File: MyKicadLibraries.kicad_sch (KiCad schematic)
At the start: 6 parts, among them U1 radio-receiver, U2 TP4056, U3 LilygoSIMT7000G, U4 esp-01m, U5 relais_module, U6 ESP-01

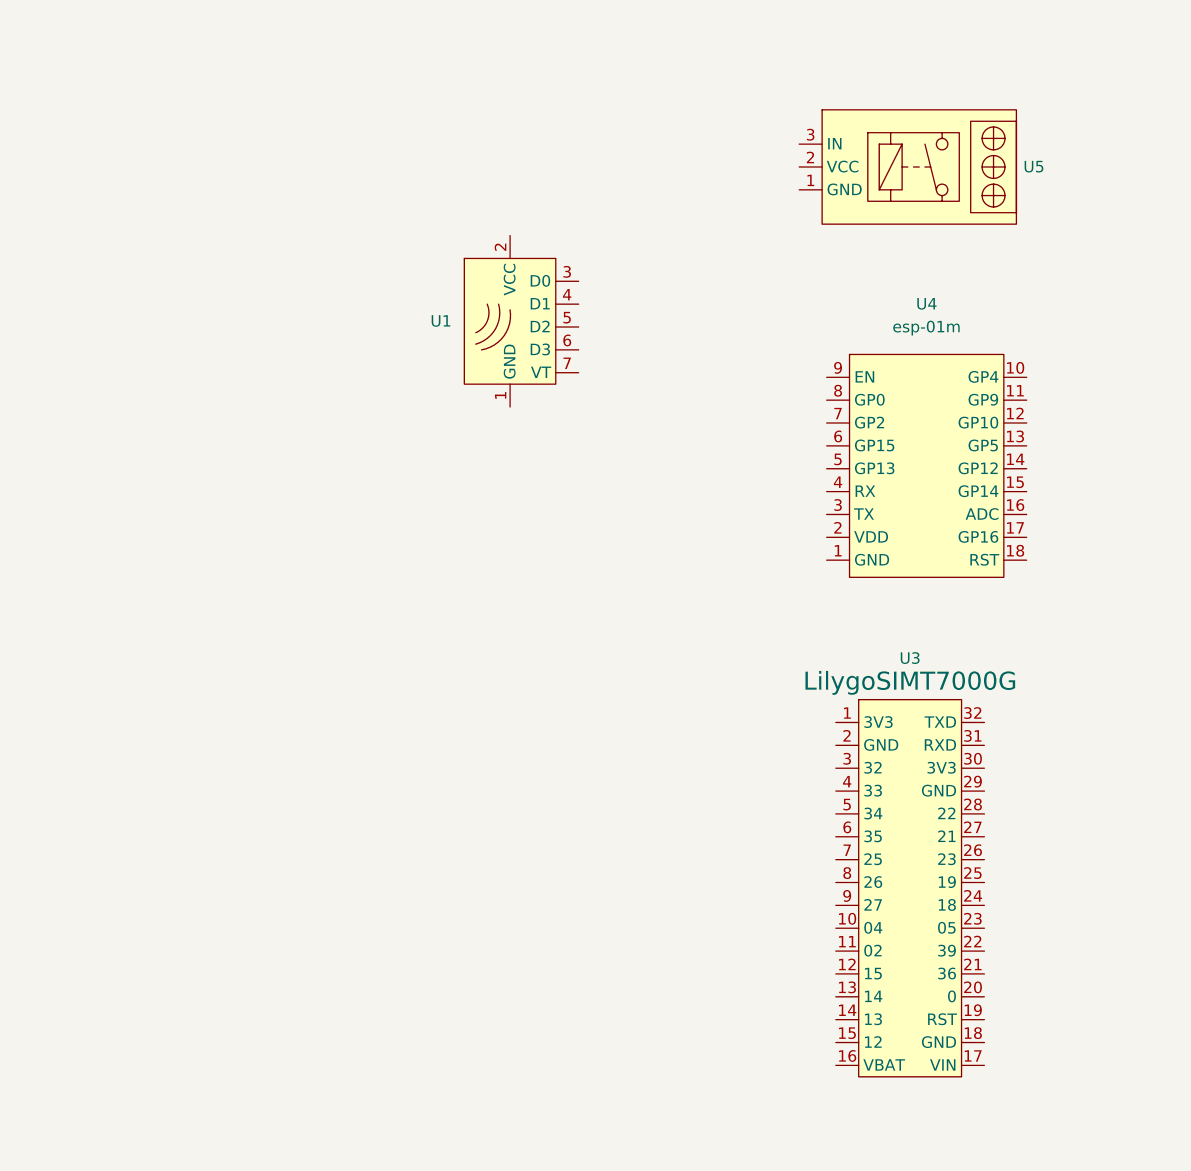
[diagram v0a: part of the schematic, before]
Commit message: Add dcdc module and add a breakout board
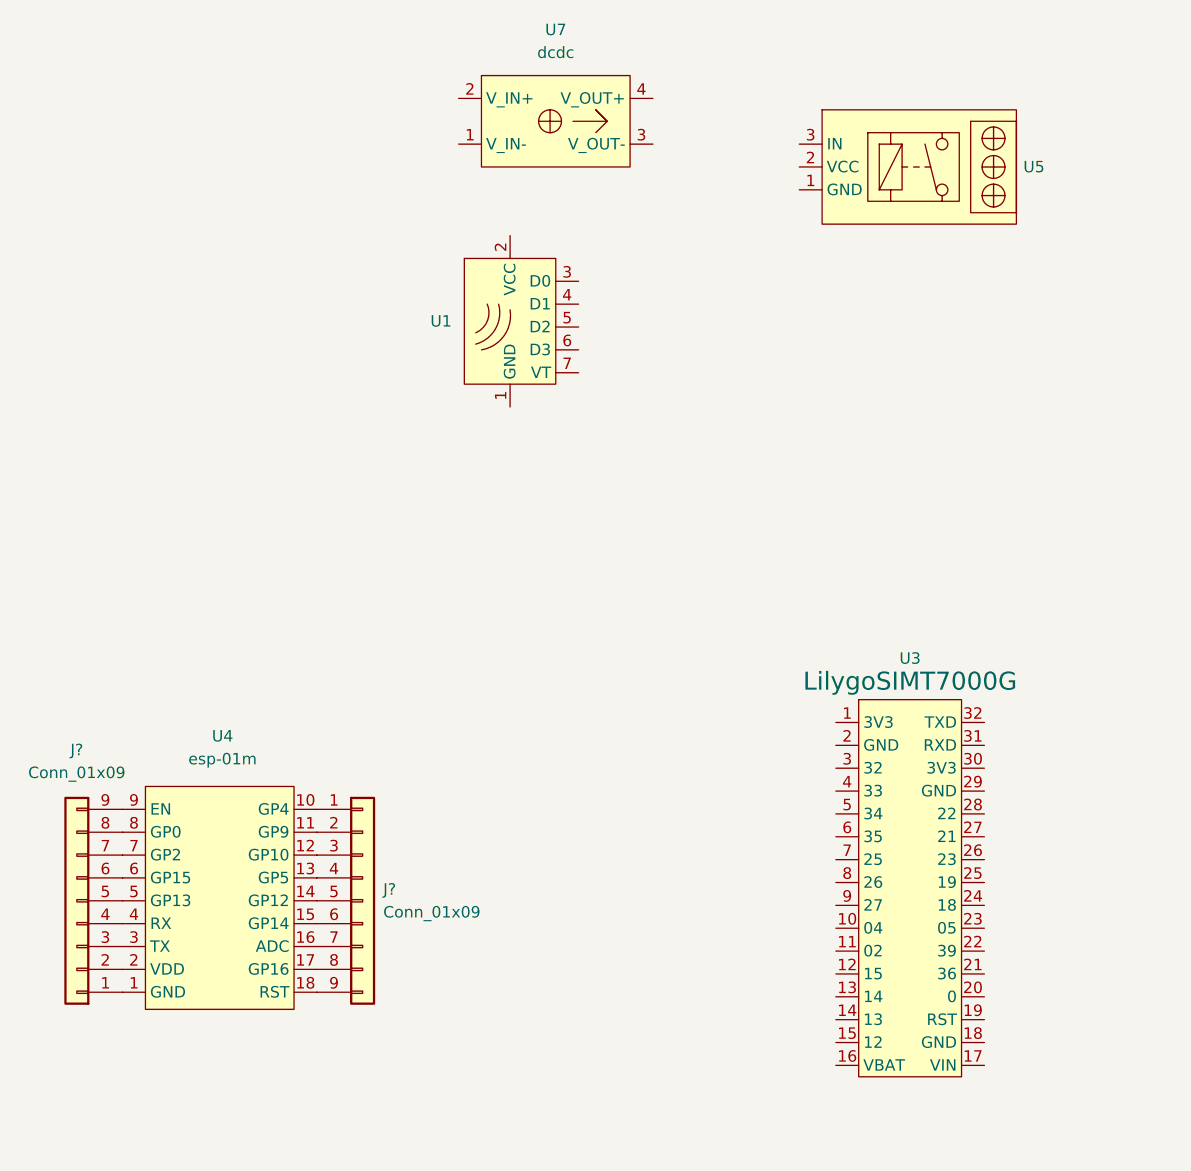
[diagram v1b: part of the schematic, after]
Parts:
- added J? (x2): Conn_01x09, connector 2.54:PinHeader_1x09_P2.54mm_Vertical, symbol connectors:Conn_01x09
- added U7: dcdc, dcdc:dcdc, symbol dcdc:dcdc
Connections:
- net at U4.1 (GND): now also J?.1 (Pin_1)
- net at U4.10 (GP4): now also J?.1 (Pin_1)
- net at U4.11 (GP9): now also J?.2 (Pin_2)
- net at U4.12 (GP10): now also J?.3 (Pin_3)
- net at U4.13 (GP5): now also J?.4 (Pin_4)
- net at U4.14 (GP12): now also J?.5 (Pin_5)
- net at U4.15 (GP14): now also J?.6 (Pin_6)
- net at U4.16 (ADC): now also J?.7 (Pin_7)
- net at U4.17 (GP16): now also J?.8 (Pin_8)
- net at U4.18 (RST): now also J?.9 (Pin_9)
- net at U4.2 (VDD): now also J?.2 (Pin_2)
- net at U4.3 (TX): now also J?.3 (Pin_3)
- net at U4.4 (RX): now also J?.4 (Pin_4)
- net at U4.5 (GP13): now also J?.5 (Pin_5)
- net at U4.6 (GP15): now also J?.6 (Pin_6)
- net at U4.7 (GP2): now also J?.7 (Pin_7)
- net at U4.8 (GP0): now also J?.8 (Pin_8)
- net at U4.9 (EN): now also J?.9 (Pin_9)
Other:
- moved on the sheet: U4
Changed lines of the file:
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@@
 (kicad_sch (version 20211123) (generator eeschema)
   (paper "A4")
-  (symbol (lib_id "esp-01m:esp-01m") (at 130.556 66.548 0) (unit 1)
-    (in_bom yes) (on_board yes) (fields_autoplaced)
-    (property "Reference" "U4" (id 0) (at 131.5085 48.26 0))
-    (property "Value" "esp-01m" (id 1) (at 131.5085 50.8 0))
-    (property "Footprint" "esp-01m:esp-01m" (id 2) (at 110.236 22.098 0)
-      (effects (font (size 1.27 1.27)) hide)
-    )
-    (property "Datasheet" "" (id 3) (at 110.236 22.098 0)
+  (symbol (lib_id "esp-01m:esp-01m") (at 52.324 114.554 0) (unit 1)
+    (in_bom yes) (on_board yes) (fields_autoplaced)
+    (property "Reference" "U4" (id 0) (at 53.2765 96.266 0))
+    (property "Value" "esp-01m" (id 1) (at 53.2765 98.806 0))
+    (property "Footprint" "esp-01m:esp-01m" (id 2) (at 32.004 70.104 0)
+      (effects (font (size 1.27 1.27)) hide)
+    )
+    (property "Datasheet" "" (id 3) (at 32.004 70.104 0)
       (effects (font (size 1.27 1.27)) hide)
     )
@@
     (pin "9")
   )
+  (symbol (lib_id "connectors:Conn_01x09") (at 68.834 114.554 0) (unit 1)
+    (in_bom yes) (on_board yes) (fields_autoplaced)
+    (property "Reference" "J?" (id 0) (at 71.12 113.2839 0)
+      (effects (font (size 1.27 1.27)) (justify left))
+    )
+    (property "Value" "Conn_01x09" (id 1) (at 71.12 115.8239 0)
+      (effects (font (size 1.27 1.27)) (justify left))
+    )
+    (property "Footprint" "connector 2.54:PinHeader_1x09_P2.54mm_Vertical" (id 2) (at 68.834 114.554 0)
+      (effects (font (size 1.27 1.27)) hide)
+    )
+    (property "Datasheet" "~" (id 3) (at 68.834 114.554 0)
+      (effects (font (size 1.27 1.27)) hide)
+    )
+    (pin "1")
+    (pin "2")
+    (pin "3")
+    (pin "4")
+    (pin "5")
+    (pin "6")
+    (pin "7")
+    (pin "8")
+    (pin "9")
+  )
   (symbol (lib_id "relais_module:relais_module") (at 131.318 33.02 0) (unit 1)
     (in_bom yes) (on_board yes) (fields_autoplaced)
@@
     (pin "2")
     (pin "3")
+  )
+  (symbol (lib_id "connectors:Conn_01x09") (at 37.084 114.554 180) (unit 1)
+    (in_bom yes) (on_board yes) (fields_autoplaced)
+    (property "Reference" "J?" (id 0) (at 37.084 97.79 0))
+    (property "Value" "Conn_01x09" (id 1) (at 37.084 100.33 0))
+    (property "Footprint" "connector 2.54:PinHeader_1x09_P2.54mm_Vertical" (id 2) (at 37.084 114.554 0)
+      (effects (font (size 1.27 1.27)) hide)
+    )
+    (property "Datasheet" "~" (id 3) (at 37.084 114.554 0)
+      (effects (font (size 1.27 1.27)) hide)
+    )
+    (pin "1")
+    (pin "2")
+    (pin "3")
+    (pin "4")
+    (pin "5")
+    (pin "6")
+    (pin "7")
+    (pin "8")
+    (pin "9")
   )
   (symbol (lib_id "ESP8266:ESP-01") (at 194.056 59.182 0) (unit 1)
@@
     (pin "7")
     (pin "8")
+  )
+  (symbol (lib_id "dcdc:dcdc") (at 89.662 27.94 0) (unit 1)
+    (in_bom yes) (on_board yes) (fields_autoplaced)
+    (property "Reference" "U7" (id 0) (at 90.297 17.78 0))
+    (property "Value" "dcdc" (id 1) (at 90.297 20.32 0))
+    (property "Footprint" "dcdc:dcdc" (id 2) (at 90.932 34.29 0)
+      (effects (font (size 1.27 1.27)) hide)
+    )
+    (property "Datasheet" "" (id 3) (at 89.662 27.94 0)
+      (effects (font (size 1.27 1.27)) hide)
+    )
+    (pin "1")
+    (pin "2")
+    (pin "3")
+    (pin "4")
   )
   (symbol (lib_id "LilygoSimT7000:LilygoSIMT7000G") (at 130.302 112.522 0) (unit 1)
@@
   )
   (symbol_instances
+    (path "/2c0dca24-f9f9-46a7-bd3a-bc66b6c0b3d7"
+      (reference "J?") (unit 1) (value "Conn_01x09") (footprint "connector 2.54:PinHeader_1x09_P2.54mm_Vertical")
+    )
+    (path "/67dc7c85-5ec5-4a6b-939d-f82942144e62"
+      (reference "J?") (unit 1) (value "Conn_01x09") (footprint "connector 2.54:PinHeader_1x09_P2.54mm_Vertical")
+    )
     (path "/e0c68c97-73e9-4f69-ab89-b954fe74c49d"
       (reference "U1") (unit 1) (value "radio-receiver") (footprint "radio-receiver:radio-receiver")
@@
       (reference "U6") (unit 1) (value "ESP-01") (footprint "ESP8266:ESP-01")
     )
-  )
+    (path "/bd2056bf-ccb9-41f7-9556-543860946181"
+      (reference "U7") (unit 1) (value "dcdc") (footprint "dcdc:dcdc")
+    )
+  )

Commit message: Finish break out board
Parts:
- gave numbers to parts that had none: 2
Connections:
- net GND: now reaches J1.1 (Pin_1), U4.1 (GND)
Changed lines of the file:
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@@
 (kicad_sch (version 20211123) (generator eeschema)
   (paper "A4")
+  (global_label "GND" (shape input) (at 42.164 124.714 270) (fields_autoplaced)
+    (effects (font (size 1.27 1.27)) (justify right))
+    (property "Intersheet References" "${INTERSHEET_REFS}" (id 0) (at 42.0846 130.9976 90)
+      (effects (font (size 1.27 1.27)) (justify right) hide)
+    )
+  )
   (symbol (lib_id "esp-01m:esp-01m") (at 52.324 114.554 0) (unit 1)
     (in_bom yes) (on_board yes) (fields_autoplaced)
@@
   (symbol (lib_id "connectors:Conn_01x09") (at 68.834 114.554 0) (unit 1)
     (in_bom yes) (on_board yes) (fields_autoplaced)
-    (property "Reference" "J?" (id 0) (at 71.12 113.2839 0)
+    (property "Reference" "J2" (id 0) (at 71.12 113.2839 0)
       (effects (font (size 1.27 1.27)) (justify left))
     )
@@
   (symbol (lib_id "connectors:Conn_01x09") (at 37.084 114.554 180) (unit 1)
     (in_bom yes) (on_board yes) (fields_autoplaced)
-    (property "Reference" "J?" (id 0) (at 37.084 97.79 0))
+    (property "Reference" "J1" (id 0) (at 37.084 97.79 0))
     (property "Value" "Conn_01x09" (id 1) (at 37.084 100.33 0))
     (property "Footprint" "connector 2.54:PinHeader_1x09_P2.54mm_Vertical" (id 2) (at 37.084 114.554 0)
@@
   )
   (symbol_instances
+    (path "/67dc7c85-5ec5-4a6b-939d-f82942144e62"
+      (reference "J1") (unit 1) (value "Conn_01x09") (footprint "connector 2.54:PinHeader_1x09_P2.54mm_Vertical")
+    )
     (path "/2c0dca24-f9f9-46a7-bd3a-bc66b6c0b3d7"
-      (reference "J?") (unit 1) (value "Conn_01x09") (footprint "connector 2.54:PinHeader_1x09_P2.54mm_Vertical")
-    )
-    (path "/67dc7c85-5ec5-4a6b-939d-f82942144e62"
-      (reference "J?") (unit 1) (value "Conn_01x09") (footprint "connector 2.54:PinHeader_1x09_P2.54mm_Vertical")
+      (reference "J2") (unit 1) (value "Conn_01x09") (footprint "connector 2.54:PinHeader_1x09_P2.54mm_Vertical")
     )
     (path "/e0c68c97-73e9-4f69-ab89-b954fe74c49d"

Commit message: Add project
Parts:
- removed J1, J2: Conn_01x09, connector 2.54:PinHeader_1x09_P2.54mm_Vertical, symbol connectors:Conn_01x09
- added J3: POGO Pins, magnetic-pogo:magnetic-pogo, symbol Connector_Generic:Conn_01x04
- added SW1: SW_Push, schurter-switch:schurter-switch, symbol Switch:SW_Push
- added U8: mems-mic, mems-mic:mems-mic, symbol mems-mic:mems-mic
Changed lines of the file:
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@@
-    (pin "9")
-  )
-  (symbol (lib_id "connectors:Conn_01x09") (at 68.834 114.554 0) (unit 1)
-    (in_bom yes) (on_board yes) (fields_autoplaced)
-    (property "Reference" "J2" (id 0) (at 71.12 113.2839 0)
-      (effects (font (size 1.27 1.27)) (justify left))
-    )
-    (property "Value" "Conn_01x09" (id 1) (at 71.12 115.8239 0)
-      (effects (font (size 1.27 1.27)) (justify left))
-    )
-    (property "Footprint" "connector 2.54:PinHeader_1x09_P2.54mm_Vertical" (id 2) (at 68.834 114.554 0)
-      (effects (font (size 1.27 1.27)) hide)
-    )
-    (property "Datasheet" "~" (id 3) (at 68.834 114.554 0)
-      (effects (font (size 1.27 1.27)) hide)
-    )
-    (pin "1")
-    (pin "2")
-    (pin "3")
-    (pin "4")
-    (pin "5")
-    (pin "6")
-    (pin "7")
-    (pin "8")
     (pin "9")
   )
@@
     (pin "3")
   )
-  (symbol (lib_id "connectors:Conn_01x09") (at 37.084 114.554 180) (unit 1)
-    (in_bom yes) (on_board yes) (fields_autoplaced)
-    (property "Reference" "J1" (id 0) (at 37.084 97.79 0))
-    (property "Value" "Conn_01x09" (id 1) (at 37.084 100.33 0))
-    (property "Footprint" "connector 2.54:PinHeader_1x09_P2.54mm_Vertical" (id 2) (at 37.084 114.554 0)
-      (effects (font (size 1.27 1.27)) hide)
-    )
-    (property "Datasheet" "~" (id 3) (at 37.084 114.554 0)
-      (effects (font (size 1.27 1.27)) hide)
-    )
-    (pin "1")
-    (pin "2")
-    (pin "3")
-    (pin "4")
-    (pin "5")
-    (pin "6")
-    (pin "7")
-    (pin "8")
-    (pin "9")
+  (symbol (lib_id "Switch:SW_Push") (at 196.85 85.09 0) (unit 1)
+    (in_bom yes) (on_board yes) (fields_autoplaced)
+    (property "Reference" "SW1" (id 0) (at 196.85 77.47 0))
+    (property "Value" "SW_Push" (id 1) (at 196.85 80.01 0))
+    (property "Footprint" "schurter-switch:schurter-switch" (id 2) (at 196.85 80.01 0)
+      (effects (font (size 1.27 1.27)) hide)
+    )
+    (property "Datasheet" "~" (id 3) (at 196.85 80.01 0)
+      (effects (font (size 1.27 1.27)) hide)
+    )
+    (pin "1")
+    (pin "2")
   )
   (symbol (lib_id "ESP8266:ESP-01") (at 194.056 59.182 0) (unit 1)
@@
     (pin "7")
     (pin "8")
+  )
+  (symbol (lib_id "mems-mic:mems-mic") (at 189.992 107.95 0) (unit 1)
+    (in_bom yes) (on_board yes) (fields_autoplaced)
+    (property "Reference" "U8" (id 0) (at 205.74 103.6193 0))
+    (property "Value" "mems-mic" (id 1) (at 205.74 106.1593 0))
+    (property "Footprint" "mems-mic:mems-mic" (id 2) (at 202.057 114.935 0)
+      (effects (font (size 1.27 1.27)) hide)
+    )
+    (property "Datasheet" "" (id 3) (at 212.852 123.19 0)
+      (effects (font (size 1.27 1.27)) hide)
+    )
+    (pin "1")
+    (pin "2")
+    (pin "3")
+    (pin "4")
+    (pin "5")
+    (pin "6")
   )
   (symbol (lib_id "dcdc:dcdc") (at 89.662 27.94 0) (unit 1)
@@
     (pin "9")
   )
+  (symbol (lib_id "Connector_Generic:Conn_01x04") (at 215.646 81.534 0) (unit 1)
+    (in_bom yes) (on_board yes) (fields_autoplaced)
+    (property "Reference" "J3" (id 0) (at 218.44 81.5339 0)
+      (effects (font (size 1.27 1.27)) (justify left))
+    )
+    (property "Value" "POGO Pins" (id 1) (at 218.44 84.0739 0)
+      (effects (font (size 1.27 1.27)) (justify left))
+    )
+    (property "Footprint" "magnetic-pogo:magnetic-pogo" (id 2) (at 215.646 81.534 0)
+      (effects (font (size 1.27 1.27)) hide)
+    )
+    (property "Datasheet" "~" (id 3) (at 215.646 81.534 0)
+      (effects (font (size 1.27 1.27)) hide)
+    )
+    (pin "1")
+    (pin "2")
+    (pin "3")
+    (pin "4")
+  )
   (symbol (lib_id "TP4056:TP4056") (at 129.286 159.258 0) (unit 1)
     (in_bom yes) (on_board yes) (fields_autoplaced)
@@
   )
   (symbol_instances
-    (path "/67dc7c85-5ec5-4a6b-939d-f82942144e62"
-      (reference "J1") (unit 1) (value "Conn_01x09") (footprint "connector 2.54:PinHeader_1x09_P2.54mm_Vertical")
-    )
-    (path "/2c0dca24-f9f9-46a7-bd3a-bc66b6c0b3d7"
-      (reference "J2") (unit 1) (value "Conn_01x09") (footprint "connector 2.54:PinHeader_1x09_P2.54mm_Vertical")
+    (path "/d4fddbda-e8d3-4c98-8244-5fdce877fc17"
+      (reference "J3") (unit 1) (value "POGO Pins") (footprint "magnetic-pogo:magnetic-pogo")
+    )
+    (path "/6445adad-5a95-43f1-96c0-6d3c8743f8cf"
+      (reference "SW1") (unit 1) (value "SW_Push") (footprint "schurter-switch:schurter-switch")
     )
     (path "/e0c68c97-73e9-4f69-ab89-b954fe74c49d"
@@
       (reference "U7") (unit 1) (value "dcdc") (footprint "dcdc:dcdc")
     )
-  )
+    (path "/a066a052-34b5-4bdd-9860-00e72b3cf061"
+      (reference "U8") (unit 1) (value "mems-mic") (footprint "mems-mic:mems-mic")
+    )
+  )

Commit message: Update neopixel library
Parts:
- added LIN1: LEDs_In, neopixel-strip:neopixel-strip, symbol neopixel-strip:LEDs_In
- added LOUT1: LEDs_Out, neopixel-strip:neopixel-strip, symbol neopixel-strip:LEDs_Out
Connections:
- new net: LIN1.1 (VCC), LOUT1.1 (VCC)
- new net: LIN1.3 (GND), LOUT1.3 (GND)
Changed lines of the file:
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@@
 (kicad_sch (version 20211123) (generator eeschema)
   (paper "A4")
+  (wire (pts (xy 36.83 45.72) (xy 38.1 45.72))
+    (stroke (width 0) (type default) (color 0 0 0 0))
+  )
+  (wire (pts (xy 36.83 40.64) (xy 38.1 40.64))
+    (stroke (width 0) (type default) (color 0 0 0 0))
+  )
   (global_label "GND" (shape input) (at 42.164 124.714 270) (fields_autoplaced)
     (effects (font (size 1.27 1.27)) (justify right))
@@
     (pin "2")
   )
+  (symbol (lib_id "neopixel-strip:LEDs_In") (at 29.21 43.18 0) (unit 1)
+    (in_bom yes) (on_board yes) (fields_autoplaced)
+    (property "Reference" "LIN1" (id 0) (at 29.337 36.83 0))
+    (property "Value" "LEDs_In" (id 1) (at 29.21 48.26 0)
+      (effects (font (size 1.27 1.27)) hide)
+    )
+    (property "Footprint" "neopixel-strip:neopixel-strip" (id 2) (at 30.48 50.8 0)
+      (effects (font (size 1.27 1.27)) hide)
+    )
+    (property "Datasheet" "" (id 3) (at 27.432 35.56 0)
+      (effects (font (size 1.27 1.27)) hide)
+    )
+    (pin "1")
+    (pin "2")
+    (pin "3")
+  )
   (symbol (lib_id "ESP8266:ESP-01") (at 194.056 59.182 0) (unit 1)
     (in_bom yes) (on_board yes) (fields_autoplaced)
@@
     (pin "5")
     (pin "6")
+  )
+  (symbol (lib_id "neopixel-strip:LEDs_Out") (at 45.72 44.45 0) (unit 1)
+    (in_bom yes) (on_board yes) (fields_autoplaced)
+    (property "Reference" "LOUT1" (id 0) (at 52.07 43.1799 0)
+      (effects (font (size 1.27 1.27)) (justify left))
+    )
+    (property "Value" "LEDs_Out" (id 1) (at 45.72 38.354 0)
+      (effects (font (size 1.27 1.27)) hide)
+    )
+    (property "Footprint" "neopixel-strip:neopixel-strip" (id 2) (at 43.942 36.83 0)
+      (effects (font (size 1.27 1.27)) hide)
+    )
+    (property "Datasheet" "" (id 3) (at 43.942 36.83 0)
+      (effects (font (size 1.27 1.27)) hide)
+    )
+    (pin "1")
+    (pin "2")
+    (pin "3")
   )
   (symbol (lib_id "dcdc:dcdc") (at 89.662 27.94 0) (unit 1)
@@
       (reference "J3") (unit 1) (value "POGO Pins") (footprint "magnetic-pogo:magnetic-pogo")
     )
+    (path "/93625391-d5f1-4afc-86f7-69a3da3b5437"
+      (reference "LIN1") (unit 1) (value "LEDs_In") (footprint "neopixel-strip:neopixel-strip")
+    )
+    (path "/a1ca8951-e4d0-4af5-bb99-86716192eefe"
+      (reference "LOUT1") (unit 1) (value "LEDs_Out") (footprint "neopixel-strip:neopixel-strip")
+    )
     (path "/6445adad-5a95-43f1-96c0-6d3c8743f8cf"

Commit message: Add new modules
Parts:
- added J1, J2: Conn_01x08, Connector_PinHeader_2.54mm:PinHeader_1x08_P2.54mm_Vertical, symbol Connector_Generic:Conn_01x08
- added J4: c8-inlet, c8-inlet:c8-inlet, symbol c8-inlet:c8-inlet
- added J5: FTDI, Connector_PinHeader_2.54mm:PinHeader_1x06_P2.54mm_Horizontal, symbol ftdi-connector:FTDI
- added U10: rdm-6300, rdm-6300:rdm-6300, symbol rdm-6300:rdm-6300
- added U9: ESP-12E, ESP8266:ESP-12E, symbol ESP8266:ESP-12E
- SW1: value SW_Push -> Schurter Switch
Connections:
- net GND: now also U10.2 (GND)
- new net: J2.1 (Pin_1), U9.9 (GND)
- new net: J2.2 (Pin_2), U9.10 (GPIO15)
- new net: J2.3 (Pin_3), U9.11 (GPIO2)
- new net: J2.4 (Pin_4), U9.12 (GPIO0)
- new net: J2.5 (Pin_5), U9.13 (GPIO4)
- new net: J2.6 (Pin_6), U9.14 (GPIO5)
- new net: J2.7 (Pin_7), U9.15 (RXD)
- new net: J2.8 (Pin_8), U9.16 (TXD)
- new net: J1.1 (Pin_1), U9.1 (REST)
- new net: J1.2 (Pin_2), U9.2 (ADC)
- new net: J1.3 (Pin_3), U9.3 (CH_PD)
- new net: J1.4 (Pin_4), U9.4 (GPIO16)
- new net: J1.5 (Pin_5), U9.5 (GPIO14)
- new net: J1.6 (Pin_6), U9.6 (GPIO12)
- new net: J1.7 (Pin_7), U9.7 (GPIO13)
- new net: J1.8 (Pin_8), U9.8 (VCC)
- new net +5V: U10.1 (VCC)
- no-connect marks 0 -> 3
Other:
- moved on the sheet: U1, U4
